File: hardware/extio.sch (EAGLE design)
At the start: 45 parts, among them IC1 PCF8574P, Q1 IRLZ44N, Q2 IRLZ44N, Q3 IRLZ44N, Q4 IRLZ44N, Q5 IRLZ44N, Q6 IRLZ44N, Q7 IRLZ44N, Q8 IRLZ44N

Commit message: extio board
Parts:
- added C4: 1uF, resistor:CPOL-EUTT2D4
- D1, D2, D3, D4, D5, D6, D7, D8: device gate433:ZENER-DIODEZD-5 -> gate433:ZENER-DIODESOD80C
- R1, R10, R11, R12, R13, R14, R15, R16, R2, R3, R4, R5, R6, R7, R8, R9: device resistor:R-EU_0204_5 -> resistor:R-EU_R0603
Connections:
- removed net N$58: X1-10.KL
- net +12V: now also X1-10.KL
- net N$69: now also C4.+
- net N$71: now also C4.-

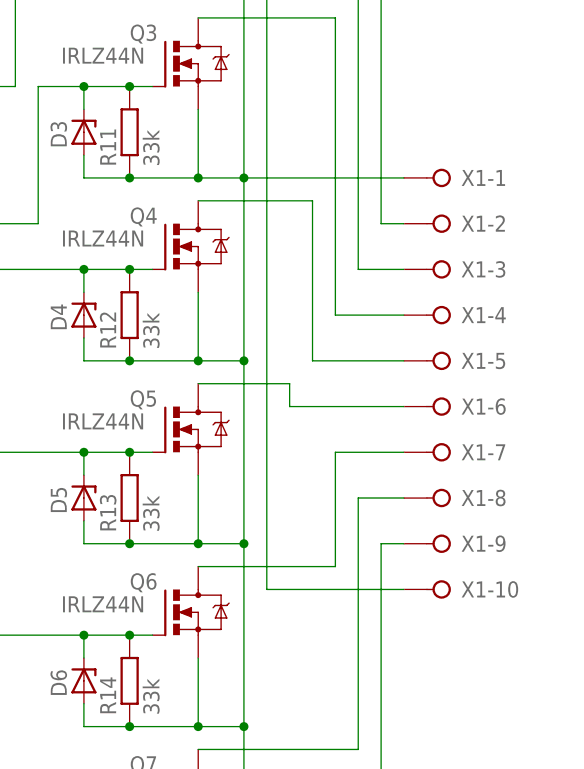
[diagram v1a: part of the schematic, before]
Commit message: extio connector fix
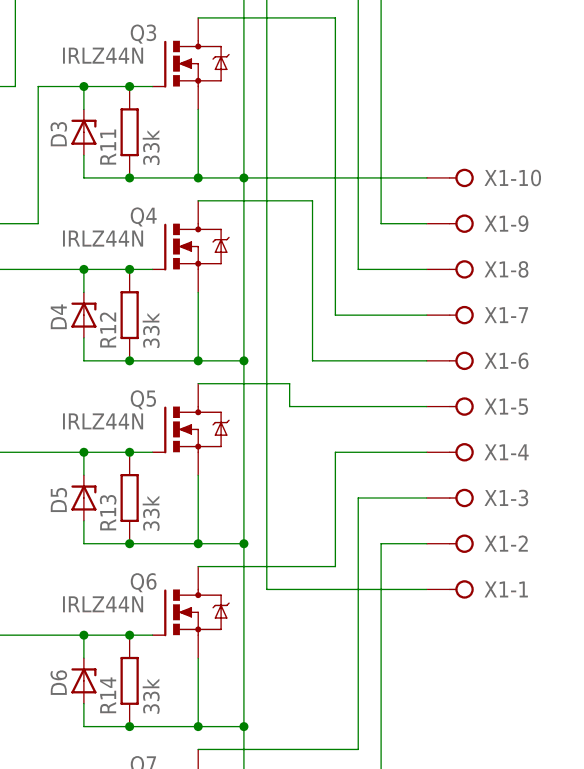
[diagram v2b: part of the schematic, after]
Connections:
- net +12V: now also X1-1.KL; no longer X1-10.KL
- net N$20: now also X1-9.KL; no longer X1-2.KL
- net N$67: now also X1-8.KL; no longer X1-3.KL
- net N$72: now also X1-7.KL; no longer X1-4.KL
- net N$77: now also X1-6.KL; no longer X1-5.KL
- net N$81: now also X1-5.KL; no longer X1-6.KL
- net N$85: now also X1-4.KL; no longer X1-7.KL
- net N$89: now also X1-3.KL; no longer X1-8.KL
- net N$93: now also X1-2.KL; no longer X1-9.KL
- net PE: now also X1-10.KL; no longer X1-1.KL
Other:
- moved on the sheet: X1-1, X1-10, X1-2, X1-3, X1-4, X1-5, X1-6, X1-7, X1-8, X1-9
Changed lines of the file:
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@@
 <instance part="P+1" gate="1" x="157.48" y="180.34"/>
 <instance part="PE1" gate="M" x="187.96" y="10.16"/>
-<instance part="X1" gate="-1" x="210.82" y="114.3" rot="MR0"/>
-<instance part="X1" gate="-2" x="210.82" y="109.22" rot="MR0"/>
-<instance part="X1" gate="-3" x="210.82" y="104.14" rot="MR0"/>
-<instance part="X1" gate="-4" x="210.82" y="99.06" rot="MR0"/>
-<instance part="X1" gate="-5" x="210.82" y="93.98" rot="MR0"/>
-<instance part="X1" gate="-6" x="210.82" y="88.9" rot="MR0"/>
-<instance part="X1" gate="-7" x="210.82" y="83.82" rot="MR0"/>
-<instance part="X1" gate="-8" x="210.82" y="78.74" rot="MR0"/>
-<instance part="X1" gate="-9" x="210.82" y="73.66" rot="MR0"/>
-<instance part="X1" gate="-10" x="210.82" y="68.58" rot="MR0"/>
+<instance part="X1" gate="-1" x="213.36" y="68.58" rot="R180"/>
+<instance part="X1" gate="-2" x="213.36" y="73.66" rot="R180"/>
+<instance part="X1" gate="-3" x="213.36" y="78.74" rot="R180"/>
+<instance part="X1" gate="-4" x="213.36" y="83.82" rot="R180"/>
+<instance part="X1" gate="-5" x="213.36" y="88.9" rot="R180"/>
+<instance part="X1" gate="-6" x="213.36" y="93.98" rot="R180"/>
+<instance part="X1" gate="-7" x="213.36" y="99.06" rot="R180"/>
+<instance part="X1" gate="-8" x="213.36" y="104.14" rot="R180"/>
+<instance part="X1" gate="-9" x="213.36" y="109.22" rot="R180"/>
+<instance part="X1" gate="-10" x="213.36" y="114.3" rot="R180"/>
 <instance part="RN1" gate="1" x="33.02" y="149.86" rot="R270"/>
 <instance part="Q1" gate="G$1" x="180.34" y="167.64" smashed="yes">
@@
 <segment>
 <pinref part="Q1" gate="G$1" pin="D"/>
-<pinref part="X1" gate="-2" pin="KL"/>
-<wire x1="205.74" y1="109.22" x2="203.2" y2="109.22" width="0.1524" layer="91"/>
 <wire x1="203.2" y1="109.22" x2="203.2" y2="172.72" width="0.1524" layer="91"/>
 <wire x1="203.2" y1="172.72" x2="182.88" y2="172.72" width="0.1524" layer="91"/>
+<pinref part="X1" gate="-9" pin="KL"/>
+<wire x1="203.2" y1="109.22" x2="208.28" y2="109.22" width="0.1524" layer="91"/>
 </segment>
 </net>
@@
 <wire x1="134.62" y1="144.78" x2="157.48" y2="144.78" width="0.1524" layer="91"/>
 <junction x="157.48" y="144.78"/>
-<pinref part="X1" gate="-10" pin="KL"/>
-<wire x1="205.74" y1="68.58" x2="190.5" y2="68.58" width="0.1524" layer="91"/>
 <wire x1="190.5" y1="68.58" x2="190.5" y2="175.26" width="0.1524" layer="91"/>
 <wire x1="190.5" y1="175.26" x2="157.48" y2="175.26" width="0.1524" layer="91"/>
 <junction x="157.48" y="175.26"/>
+<pinref part="X1" gate="-1" pin="KL"/>
+<wire x1="190.5" y1="68.58" x2="208.28" y2="68.58" width="0.1524" layer="91"/>
 </segment>
 </net>
@@
 <segment>
 <pinref part="Q2" gate="G$1" pin="D"/>
-<pinref part="X1" gate="-3" pin="KL"/>
-<wire x1="205.74" y1="104.14" x2="200.66" y2="104.14" width="0.1524" layer="91"/>
 <wire x1="200.66" y1="104.14" x2="200.66" y2="152.4" width="0.1524" layer="91"/>
 <wire x1="200.66" y1="152.4" x2="182.88" y2="152.4" width="0.1524" layer="91"/>
+<pinref part="X1" gate="-8" pin="KL"/>
+<wire x1="200.66" y1="104.14" x2="208.28" y2="104.14" width="0.1524" layer="91"/>
 </segment>
 </net>
@@
 <segment>
 <pinref part="Q3" gate="G$1" pin="D"/>
-<pinref part="X1" gate="-4" pin="KL"/>
-<wire x1="205.74" y1="99.06" x2="198.12" y2="99.06" width="0.1524" layer="91"/>
 <wire x1="198.12" y1="99.06" x2="198.12" y2="132.08" width="0.1524" layer="91"/>
 <wire x1="198.12" y1="132.08" x2="182.88" y2="132.08" width="0.1524" layer="91"/>
+<pinref part="X1" gate="-7" pin="KL"/>
+<wire x1="198.12" y1="99.06" x2="208.28" y2="99.06" width="0.1524" layer="91"/>
 </segment>
 </net>
@@
 <segment>
 <pinref part="Q4" gate="G$1" pin="D"/>
-<pinref part="X1" gate="-5" pin="KL"/>
-<wire x1="205.74" y1="93.98" x2="195.58" y2="93.98" width="0.1524" layer="91"/>
 <wire x1="195.58" y1="93.98" x2="195.58" y2="111.76" width="0.1524" layer="91"/>
 <wire x1="195.58" y1="111.76" x2="182.88" y2="111.76" width="0.1524" layer="91"/>
+<pinref part="X1" gate="-6" pin="KL"/>
+<wire x1="195.58" y1="93.98" x2="208.28" y2="93.98" width="0.1524" layer="91"/>
 </segment>
 </net>
@@
 <segment>
 <pinref part="Q5" gate="G$1" pin="D"/>
-<pinref part="X1" gate="-6" pin="KL"/>
-<wire x1="205.74" y1="88.9" x2="193.04" y2="88.9" width="0.1524" layer="91"/>
 <wire x1="193.04" y1="88.9" x2="193.04" y2="91.44" width="0.1524" layer="91"/>
 <wire x1="193.04" y1="91.44" x2="182.88" y2="91.44" width="0.1524" layer="91"/>
+<pinref part="X1" gate="-5" pin="KL"/>
+<wire x1="193.04" y1="88.9" x2="208.28" y2="88.9" width="0.1524" layer="91"/>
 </segment>
 </net>
@@
 <segment>
 <pinref part="Q6" gate="G$1" pin="D"/>
-<pinref part="X1" gate="-7" pin="KL"/>
-<wire x1="205.74" y1="83.82" x2="198.12" y2="83.82" width="0.1524" layer="91"/>
 <wire x1="198.12" y1="83.82" x2="198.12" y2="71.12" width="0.1524" layer="91"/>
 <wire x1="198.12" y1="71.12" x2="182.88" y2="71.12" width="0.1524" layer="91"/>
+<pinref part="X1" gate="-4" pin="KL"/>
+<wire x1="198.12" y1="83.82" x2="208.28" y2="83.82" width="0.1524" layer="91"/>
 </segment>
 </net>
@@
 <segment>
 <pinref part="Q7" gate="G$1" pin="D"/>
-<pinref part="X1" gate="-8" pin="KL"/>
-<wire x1="205.74" y1="78.74" x2="200.66" y2="78.74" width="0.1524" layer="91"/>
 <wire x1="200.66" y1="78.74" x2="200.66" y2="50.8" width="0.1524" layer="91"/>
 <wire x1="200.66" y1="50.8" x2="182.88" y2="50.8" width="0.1524" layer="91"/>
+<pinref part="X1" gate="-3" pin="KL"/>
+<wire x1="200.66" y1="78.74" x2="208.28" y2="78.74" width="0.1524" layer="91"/>
 </segment>
 </net>
@@
 <segment>
 <pinref part="Q8" gate="G$1" pin="D"/>
-<pinref part="X1" gate="-9" pin="KL"/>
-<wire x1="205.74" y1="73.66" x2="203.2" y2="73.66" width="0.1524" layer="91"/>
 <wire x1="203.2" y1="73.66" x2="203.2" y2="30.48" width="0.1524" layer="91"/>
 <wire x1="203.2" y1="30.48" x2="182.88" y2="30.48" width="0.1524" layer="91"/>
+<pinref part="X1" gate="-2" pin="KL"/>
+<wire x1="203.2" y1="73.66" x2="208.28" y2="73.66" width="0.1524" layer="91"/>
 </segment>
 </net>
@@
 <junction x="182.88" y="114.3"/>
 <junction x="187.96" y="114.3"/>
-<pinref part="X1" gate="-1" pin="KL"/>
-<wire x1="205.74" y1="114.3" x2="187.96" y2="114.3" width="0.1524" layer="91"/>
 <pinref part="PE1" gate="M" pin="PE"/>
 <junction x="187.96" y="12.7"/>
-</segment>
-</net>
+<pinref part="X1" gate="-10" pin="KL"/>
+<wire x1="208.28" y1="114.3" x2="187.96" y2="114.3" width="0.1524" layer="91"/>
+</segment>
+</net>

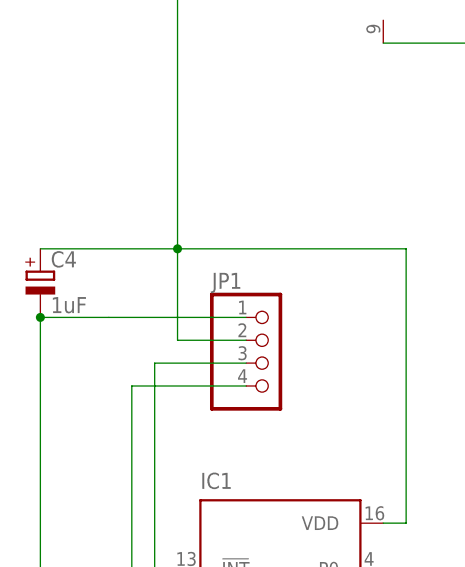
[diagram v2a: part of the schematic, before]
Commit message: extio C1 to SMD
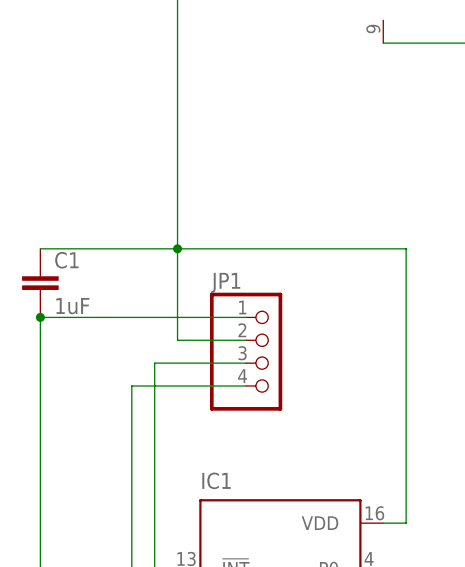
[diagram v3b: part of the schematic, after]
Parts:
- removed C4: 1uF, resistor:CPOL-EUTT2D4
- added C1: 1uF, resistor:C-EUC0603
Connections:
- net N$69: now also C1.1; no longer C4.+
- net N$71: now also C1.2; no longer C4.-
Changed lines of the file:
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@@
 <part name="R16" library="resistor" deviceset="R-EU_" device="R0603" value="33k"/>
 <part name="D8" library="gate433" deviceset="ZENER-DIODE" device="SOD80C"/>
-<part name="C4" library="resistor" deviceset="CPOL-EU" device="TT2D4" value="1uF"/>
+<part name="C1" library="resistor" deviceset="C-EU" device="C0603" value="1uF"/>
 </parts>
 <sheets>
@@
 <instance part="R16" gate="G$1" x="175.26" y="17.78" rot="R90"/>
 <instance part="D8" gate="G$1" x="170.18" y="17.78" rot="R90"/>
-<instance part="C4" gate="G$1" x="-5.08" y="83.82"/>
+<instance part="C1" gate="G$1" x="-5.08" y="83.82"/>
 </instances>
 <busses>
@@
 <pinref part="IC1" gate="G$1" pin="VDD"/>
 <wire x1="35.56" y1="55.88" x2="33.02" y2="55.88" width="0.1524" layer="91"/>
-<pinref part="C4" gate="G$1" pin="+"/>
+<pinref part="C1" gate="G$1" pin="1"/>
 <wire x1="-5.08" y1="86.36" x2="10.16" y2="86.36" width="0.1524" layer="91"/>
 </segment>
@@
 <pinref part="JP1" gate="A" pin="1"/>
 <wire x1="2.54" y1="78.74" x2="17.78" y2="78.74" width="0.1524" layer="91"/>
-<pinref part="C4" gate="G$1" pin="-"/>
+<pinref part="C1" gate="G$1" pin="2"/>
 <wire x1="-5.08" y1="78.74" x2="-5.08" y2="38.1" width="0.1524" layer="91"/>
 <wire x1="-5.08" y1="38.1" x2="2.54" y2="38.1" width="0.1524" layer="91"/>
